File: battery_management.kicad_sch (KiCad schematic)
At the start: 20 parts, among them Q501 Q_PMOS_DGS, Q502 FS8205, U501 FS312F-G, U502 TP4056, U503 MAX17048

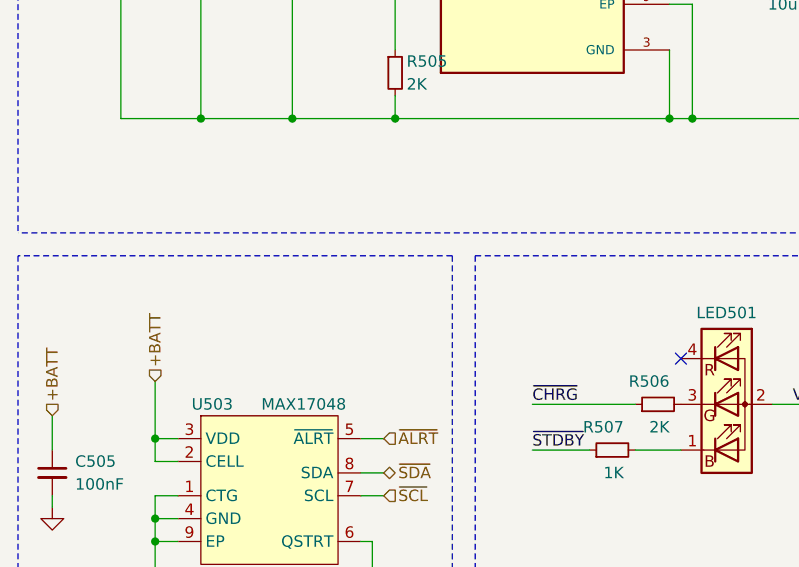
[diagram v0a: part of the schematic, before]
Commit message: add RTC, humidity and temp sensors
updated footprint paths
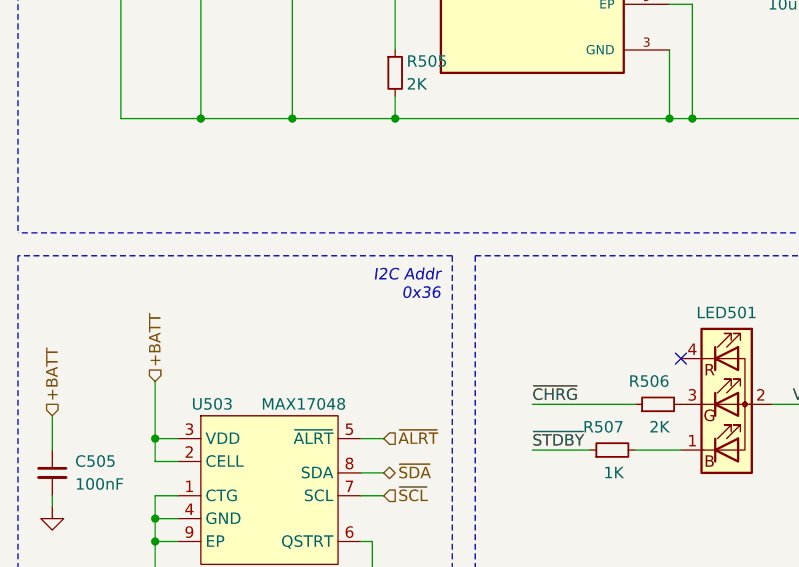
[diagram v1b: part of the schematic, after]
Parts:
- LED501: footprint User Added Footprints:LED-4_1.6x1.6x0.85P -> User Custom Footprint:LED-4_1.6x1.6x0.85P
- Q502: footprint footprints:SOT95P280X145-6N -> User Custom Footprint:SOT95P280X145-6N
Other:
- note added: "I2C Addr 0x36"
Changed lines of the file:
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@@
     (effects (font (size 2 2)) (justify right bottom))
+  )
+  (text "I2C Addr\n0x36" (at 64.77 104.14 0)
+    (effects (font (size 1.27 1.27) italic) (justify right bottom))
   )
   (text "Charger Indicator LED" (at 115.57 137.16 0)
@@
       (effects (font (size 1.27 1.27)) (justify left))
     )
-    (property "Footprint" "footprints:SOT95P280X145-6N" (at 158.75 77.47 0)
+    (property "Footprint" "User Custom Footprint:SOT95P280X145-6N" (at 158.75 77.47 0)
       (effects (font (size 1.27 1.27)) (justify left bottom) hide)
     )
@@
       (effects (font (size 1.27 1.27)) hide)
     )
-    (property "Footprint" "User Added Footprints:LED-4_1.6x1.6x0.85P" (at 96.52 116.84 0)
-      (effects (font (size 1.27 1.27)) hide)
-    )
+    (property "Footprint" "User Custom Footprint:LED-4_1.6x1.6x0.85P" (at 96.52 116.84 0)
+      (effects (font (size 1.27 1.27)) hide)
+    )

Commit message: update LCSC parts and footprints
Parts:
- U503: footprint 3rd Party:MAX17048G&plus_T10 -> User Custom Footprint:MAX17048G&plus_T10
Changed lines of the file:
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@@
       (effects (font (size 1.27 1.27)))
     )
-    (property "Footprint" "3rd Party:MAX17048G&plus_T10" (at 44.45 137.16 0)
+    (property "Footprint" "User Custom Footprint:MAX17048G&plus_T10" (at 44.45 137.16 0)
       (effects (font (size 1.27 1.27)) hide)
     )

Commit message: revise schematics
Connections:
- net ~{CHRG}: now also R507.1; no longer R506.1
- net ~{STDBY}: now also R506.1; no longer R507.1
- net at R507.2: now also LED501.4 (RK); no longer LED501.1 (BK)
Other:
- moved on the sheet: LED501, R506, R507
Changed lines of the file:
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@@
   )
   (no_connect (at 114.3 66.04))
-  (no_connect (at 91.44 110.49))
+  (no_connect (at 90.17 124.46))
   (no_connect (at 153.67 69.85))
   (no_connect (at 153.67 80.01))
@@
     (stroke (width 0) (type default))
   )
-  (wire (pts (xy 74.93 115.57) (xy 86.36 115.57))
+  (wire (pts (xy 72.39 114.3) (xy 85.09 114.3))
     (stroke (width 0) (type default))
   )
@@
     (stroke (width 0) (type dash))
   )
-  (wire (pts (xy 101.6 115.57) (xy 111.76 115.57))
+  (wire (pts (xy 100.33 119.38) (xy 110.49 119.38))
     (stroke (width 0) (type default))
   )
@@
     (stroke (width 0) (type default))
   )
-  (wire (pts (xy 86.36 120.65) (xy 91.44 120.65))
+  (wire (pts (xy 85.09 119.38) (xy 90.17 119.38))
     (stroke (width 0) (type default))
   )
@@
     (stroke (width 0) (type default))
   )
-  (wire (pts (xy 74.93 120.65) (xy 81.28 120.65))
+  (wire (pts (xy 72.39 119.38) (xy 80.01 119.38))
     (stroke (width 0) (type default))
   )
@@
     (effects (font (size 2 2)) (justify right bottom))
   )
-  (label "~{CHRG}" (at 74.93 115.57 0) (fields_autoplaced)
+  (label "~{CHRG}" (at 72.39 114.3 0) (fields_autoplaced)
     (effects (font (size 1.27 1.27)) (justify left bottom))
   )
-  (label "~{STDBY}" (at 74.93 120.65 0) (fields_autoplaced)
+  (label "~{STDBY}" (at 72.39 119.38 0) (fields_autoplaced)
     (effects (font (size 1.27 1.27)) (justify left bottom))
   )
@@
     (effects (font (size 1.27 1.27)) (justify left bottom))
   )
-  (label "VCC_LED" (at 111.76 115.57 180) (fields_autoplaced)
+  (label "VCC_LED" (at 110.49 119.38 180) (fields_autoplaced)
     (effects (font (size 1.27 1.27)) (justify right bottom))
   )
@@
     )
   )
-  (symbol (lib_id "Device:R_Small") (at 88.9 115.57 90) (unit 1)
-    (in_bom yes) (on_board yes) (dnp no)
-    (property "Reference" "R506" (at 90.17 113.03 90)
-      (effects (font (size 1.27 1.27)) (justify left))
-    )
-    (property "Value" "2K" (at 90.17 118.11 90)
-      (effects (font (size 1.27 1.27)) (justify left))
-    )
-    (property "Footprint" "Resistor_SMD:R_0805_2012Metric" (at 88.9 117.348 90)
-      (effects (font (size 1.27 1.27)) hide)
-    )
-    (property "Datasheet" "~" (at 88.9 115.57 0)
-      (effects (font (size 1.27 1.27)) hide)
-    )
-    (property "LCSC" "C17604" (at 88.9 115.57 0)
+  (symbol (lib_id "Device:R_Small") (at 82.55 119.38 90) (unit 1)
+    (in_bom yes) (on_board yes) (dnp no)
+    (property "Reference" "R506" (at 83.82 116.84 90)
+      (effects (font (size 1.27 1.27)) (justify left))
+    )
+    (property "Value" "2K" (at 83.82 121.92 90)
+      (effects (font (size 1.27 1.27)) (justify left))
+    )
+    (property "Footprint" "Resistor_SMD:R_0805_2012Metric" (at 82.55 121.158 90)
+      (effects (font (size 1.27 1.27)) hide)
+    )
+    (property "Datasheet" "~" (at 82.55 119.38 0)
+      (effects (font (size 1.27 1.27)) hide)
+    )
+    (property "LCSC" "C17604" (at 82.55 119.38 0)
       (effects (font (size 1.27 1.27)) hide)
     )
@@
     )
   )
-  (symbol (lib_id "Device:R_Small") (at 83.82 120.65 90) (unit 1)
-    (in_bom yes) (on_board yes) (dnp no)
-    (property "Reference" "R507" (at 85.09 118.11 90)
-      (effects (font (size 1.27 1.27)) (justify left))
-    )
-    (property "Value" "1K" (at 85.09 123.19 90)
-      (effects (font (size 1.27 1.27)) (justify left))
-    )
-    (property "Footprint" "Resistor_SMD:R_0805_2012Metric" (at 83.82 122.428 90)
-      (effects (font (size 1.27 1.27)) hide)
-    )
-    (property "Datasheet" "~" (at 83.82 120.65 0)
-      (effects (font (size 1.27 1.27)) hide)
-    )
-    (property "LCSC" "C17513" (at 83.82 120.65 0)
+  (symbol (lib_id "Device:R_Small") (at 87.63 114.3 90) (unit 1)
+    (in_bom yes) (on_board yes) (dnp no)
+    (property "Reference" "R507" (at 88.9 111.76 90)
+      (effects (font (size 1.27 1.27)) (justify left))
+    )
+    (property "Value" "1K" (at 88.9 116.84 90)
+      (effects (font (size 1.27 1.27)) (justify left))
+    )
+    (property "Footprint" "Resistor_SMD:R_0805_2012Metric" (at 87.63 116.078 90)
+      (effects (font (size 1.27 1.27)) hide)
+    )
+    (property "Datasheet" "~" (at 87.63 114.3 0)
+      (effects (font (size 1.27 1.27)) hide)
+    )
+    (property "LCSC" "C17513" (at 87.63 114.3 0)
       (effects (font (size 1.27 1.27)) hide)
     )
@@
     )
   )
-  (symbol (lib_id "Device:LED_BAGR") (at 96.52 115.57 0) (unit 1)
-    (in_bom yes) (on_board yes) (dnp no)
-    (property "Reference" "LED501" (at 96.52 105.41 0)
+  (symbol (lib_id "Device:LED_BAGR") (at 95.25 119.38 0) (unit 1)
+    (in_bom yes) (on_board yes) (dnp no)
+    (property "Reference" "LED501" (at 95.25 109.22 0)
       (effects (font (size 1.27 1.27)))
     )
-    (property "Value" "LED_RAGB" (at 96.52 104.14 0)
-      (effects (font (size 1.27 1.27)) hide)
-    )
-    (property "Footprint" "User Custom Footprint:LED-4_1.6x1.6x0.85P" (at 96.52 116.84 0)
-      (effects (font (size 1.27 1.27)) hide)
-    )
-    (property "Datasheet" "~" (at 96.52 116.84 0)
-      (effects (font (size 1.27 1.27)) hide)
-    )
-    (property "LCSC" "C375569" (at 96.52 115.57 0)
-      (effects (font (size 1.27 1.27)) hide)
-    )
+    (property "Value" "LED_RAGB" (at 95.25 107.95 0)
+      (effects (font (size 1.27 1.27)) hide)
+    )
+    (property "Footprint" "User Custom Footprint:LED-4_1.6x1.6x0.85P" (at 95.25 120.65 0)
+      (effects (font (size 1.27 1.27)) hide)
+    )
+    (property "Datasheet" "~" (at 95.25 120.65 0)
+      (effects (font (size 1.27 1.27)) hide)
+    )
+    (property "LCSC" "C375569" (at 95.25 119.38 0)
+      (effects (font (size 1.27 1.27)) hide)
+    )

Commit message: update pcb layout
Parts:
- removed D502: D_Schottky, Diode_SMD:D_SMA, symbol Device:D_Schottky_Small
- U502: footprint SOP127P600X175-9N -> User Custom Footprint:SOP127P600X175-9N
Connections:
- net +BATT: now also Q501.3 (D)
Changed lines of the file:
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@@
     (stroke (width 0) (type default))
   )
-  (wire (pts (xy 129.54 44.45) (xy 134.62 44.45))
+  (wire (pts (xy 129.54 44.45) (xy 139.7 44.45))
     (stroke (width 0) (type default))
   )
@@
         (path "/da21b043-c1be-47f1-86d6-d54e7594fd6d/d63a1ea6-f792-4b91-a11b-7cc51ec3a111"
           (reference "C505") (unit 1)
-        )
-      )
-    )
-  )
-  (symbol (lib_id "Device:D_Schottky_Small") (at 137.16 44.45 180) (unit 1)
-    (in_bom yes) (on_board yes) (dnp no)
-    (property "Reference" "D502" (at 135.89 41.91 0)
-      (effects (font (size 1.27 1.27)) (justify right))
-    )
-    (property "Value" "D_Schottky" (at 138.7474 41.91 90)
-      (effects (font (size 1.27 1.27)) (justify right) hide)
-    )
-    (property "Footprint" "Diode_SMD:D_SMA" (at 137.16 44.45 90)
-      (effects (font (size 1.27 1.27)) hide)
-    )
-    (property "Datasheet" "~" (at 137.16 44.45 90)
-      (effects (font (size 1.27 1.27)) hide)
-    )
-    (property "LCSC" "C2480" (at 137.16 44.45 0)
-      (effects (font (size 1.27 1.27)) hide)
-    )
-    (pin "1")
-    (pin "2")
-    (instances
-      (project "iot_playground"
-        (path "/da21b043-c1be-47f1-86d6-d54e7594fd6d/d63a1ea6-f792-4b91-a11b-7cc51ec3a111"
-          (reference "D502") (unit 1)
         )
       )
@@
       (effects (font (size 1.27 1.27)))
     )
-    (property "Footprint" "SOP127P600X175-9N" (at 64.77 83.82 0)
+    (property "Footprint" "User Custom Footprint:SOP127P600X175-9N" (at 64.77 83.82 0)
       (effects (font (size 1.27 1.27)) (justify left bottom) hide)
     )
@@
       (effects (font (size 1.27 1.27)) hide)
     )
+    (property "Mouser" "" (at 74.93 66.04 0)
+      (effects (font (size 1.27 1.27)) hide)
+    )
+    (property "DigiKey" "" (at 74.93 66.04 0)
+      (effects (font (size 1.27 1.27)) hide)
+    )
